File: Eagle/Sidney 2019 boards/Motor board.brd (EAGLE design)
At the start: 110 x 122 mm, 40 parts, among them IC2 LM2940CS-5.0_NOPB

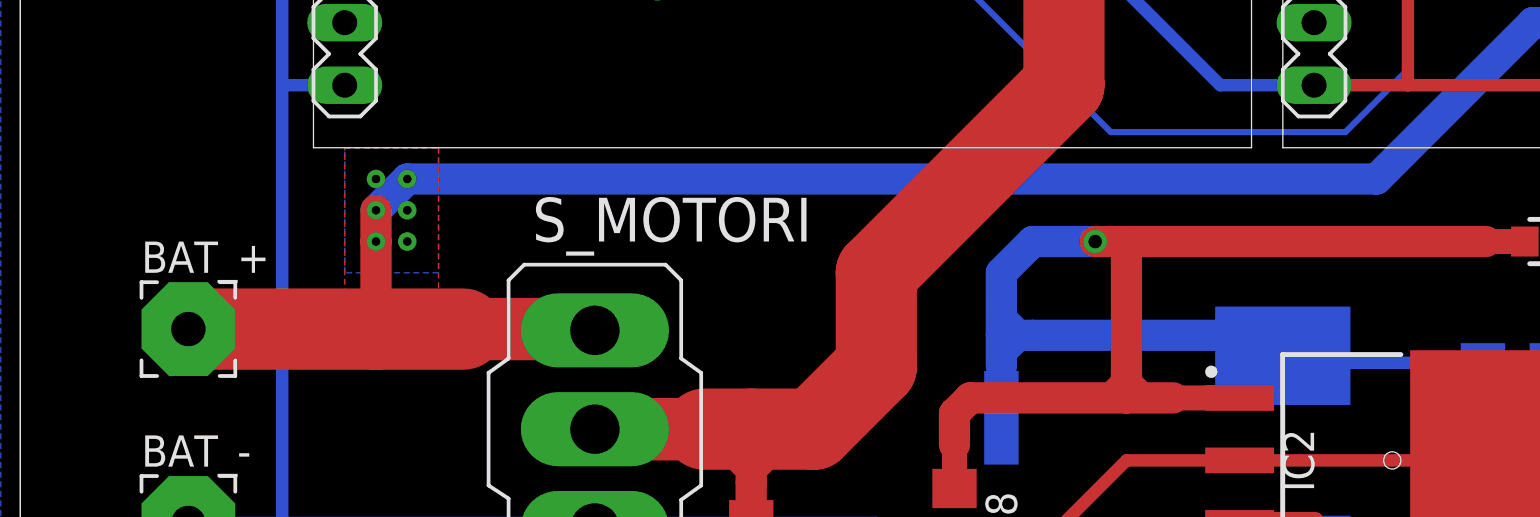
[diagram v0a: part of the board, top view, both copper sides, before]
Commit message: Fixed polygon near battery causing a short circuit
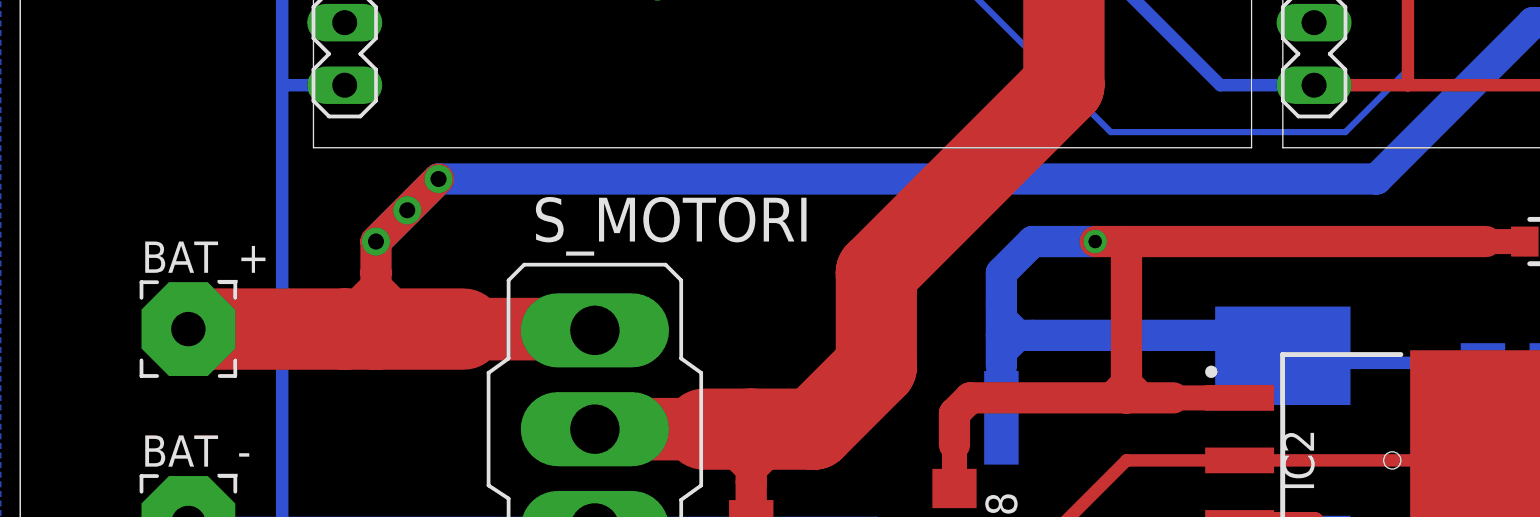
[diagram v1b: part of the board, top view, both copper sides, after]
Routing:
- net N$1: track 111.0 -> 117.8 mm
- removed copper zone on layer 1, net N$1
- removed copper zone on layer 16, net N$1
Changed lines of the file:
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@@
 <via x="55.88" y="80.01" extent="1-16" drill="0.35"/>
 <via x="114.3" y="73.66" extent="1-16" drill="0.35"/>
-<wire x1="116.84" y1="118.11" x2="105.41" y2="119.38" width="0" layer="19" extent="1-1"/>
-<wire x1="114.3" y1="73.66" x2="114.3" y2="72.39" width="0" layer="19" extent="16-16"/>
-<wire x1="90.17" y1="119.38" x2="85.09" y2="111.76" width="0" layer="19" extent="16-16"/>
-<wire x1="55.88" y1="80.01" x2="43.18" y2="81.28" width="0" layer="19" extent="1-1"/>
-<wire x1="52.07" y1="123.19" x2="58.42" y2="111.76" width="0" layer="19" extent="1-1"/>
 <via x="113.03" y="72.39" extent="1-16" drill="0.35"/>
 <via x="114.3" y="72.39" extent="1-16" drill="0.35"/>
@@
 <wire x1="116.84" y1="73.66" x2="116.84" y2="67.31" width="1.27" layer="16"/>
 <contactref element="BAT_+" pad="1"/>
-<wire x1="36.83" y1="66.294" x2="44.45" y2="66.294" width="3.302" layer="1"/>
+<wire x1="36.83" y1="66.294" x2="43.18" y2="66.294" width="3.302" layer="1"/>
+<wire x1="43.18" y1="66.294" x2="44.45" y2="66.294" width="3.302" layer="1"/>
 <wire x1="44.45" y1="66.294" x2="48.006" y2="66.294" width="3.302" layer="1"/>
 <wire x1="48.006" y1="66.294" x2="53.2892" y2="66.294" width="2.54" layer="1"/>
 <wire x1="53.2892" y1="66.294" x2="53.34" y2="66.2432" width="2.54" layer="1"/>
 <wire x1="91.44" y1="78.74" x2="85.09" y2="72.39" width="1.27" layer="16"/>
-<wire x1="44.45" y1="69.85" x2="44.45" y2="66.294" width="1.27" layer="1"/>
-<wire x1="85.09" y1="72.39" x2="45.72" y2="72.39" width="1.27" layer="16"/>
-<polygon width="0.1524" layer="1">
-<vertex x="43.18" y="73.66"/>
-<vertex x="46.99" y="73.66"/>
-<vertex x="46.99" y="67.31"/>
-<vertex x="43.18" y="67.31"/>
-</polygon>
-<polygon width="0.1524" layer="16">
-<vertex x="43.18" y="73.66"/>
-<vertex x="46.99" y="73.66"/>
-<vertex x="46.99" y="68.58"/>
-<vertex x="43.18" y="68.58"/>
-</polygon>
-<via x="45.72" y="72.39" extent="1-16" drill="0.35"/>
-<via x="44.45" y="69.85" extent="1-16" drill="0.35"/>
-<wire x1="45.72" y1="72.39" x2="44.45" y2="71.12" width="1.27" layer="16"/>
-<via x="44.45" y="71.12" extent="1-16" drill="0.35"/>
-<wire x1="44.45" y1="71.12" x2="44.45" y2="69.85" width="1.27" layer="1"/>
+<wire x1="85.09" y1="72.39" x2="46.99" y2="72.39" width="1.27" layer="16"/>
+<wire x1="46.99" y1="72.39" x2="45.72" y2="71.12" width="1.27" layer="16"/>
+<via x="44.45" y="69.85" extent="1-16" drill="0.65" diameter="1.15"/>
+<wire x1="45.72" y1="71.12" x2="44.45" y2="69.85" width="1.27" layer="16"/>
+<wire x1="44.45" y1="66.294" x2="44.45" y2="68.58" width="1.27" layer="1"/>
+<wire x1="44.45" y1="69.85" x2="44.45" y2="68.58" width="1.27" layer="1"/>
+<wire x1="44.45" y1="69.85" x2="45.72" y2="71.12" width="1.27" layer="1"/>
+<via x="46.99" y="72.39" extent="1-16" drill="0.65" diameter="1.15"/>
+<wire x1="45.72" y1="71.12" x2="46.99" y2="72.39" width="1.27" layer="1"/>
+<via x="45.72" y="71.12" extent="1-16" drill="0.65" diameter="1.15"/>
+<wire x1="43.18" y1="66.294" x2="43.18" y2="67.31" width="0.508" layer="1"/>
+<wire x1="43.18" y1="67.31" x2="44.45" y2="68.58" width="0.508" layer="1"/>
+<wire x1="44.45" y1="68.58" x2="45.212" y2="67.818" width="0.508" layer="1"/>
 </signal>
 <signal name="VCC">
@@
 <wire x1="128.27" y1="125.73" x2="100.33" y2="153.67" width="0.254" layer="16"/>
 </signal>
-<signal name="N$4">
-<via x="45.72" y="69.85" extent="1-16" drill="0.35"/>
-</signal>
-<signal name="N$5">
-<via x="45.72" y="71.12" extent="1-16" drill="0.35"/>
-</signal>
-<signal name="N$8">
-<via x="44.45" y="72.39" extent="1-16" drill="0.35"/>
-</signal>
 </signals>

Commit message: Started working on line sensors's 3.3V supply
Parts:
- added IC3: LM3940IS-3.3, LM3940IS-3.3:TO254P1435X457-4N
- moved SUPPLY2_CON 2.84 mm to (133.3, 90.2)
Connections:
- new net 3,3V/LS: IC3.3, S1.1, S2.1, S3.1, S4.1
- net +5V/S: now also IC3.1; no longer S1.1, S2.1, S3.1, S4.1
- net GND: now also IC3.2, IC3.4
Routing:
- net 3,3V/LS: track 0.00 -> 103.9 mm
- net +5V/S: track 440.5 -> 354.2 mm
- net GND: track 646.6 -> 667.6 mm
- net +5V: track 86.6 -> 85.8 mm

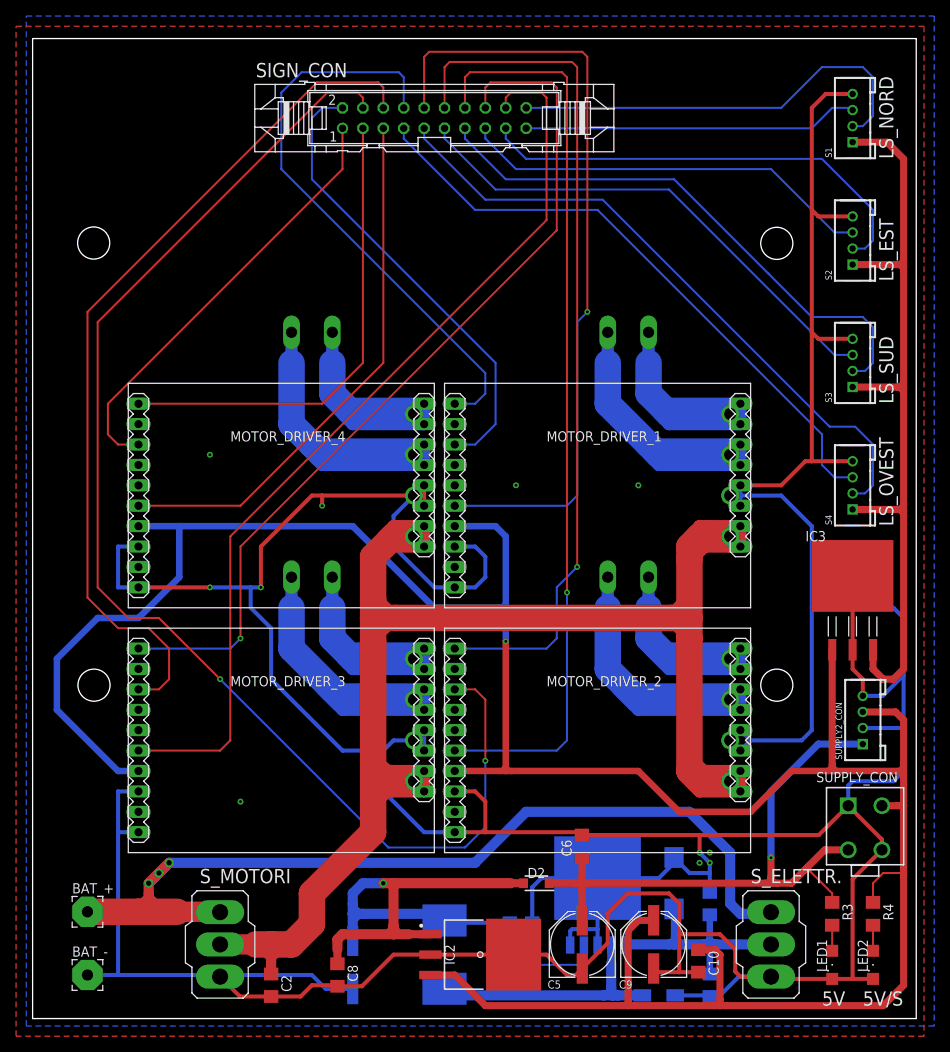
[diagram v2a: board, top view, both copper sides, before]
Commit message: Working on vias, removed empty portions of the motor board, added 3,3V LDO regulator for line sensors
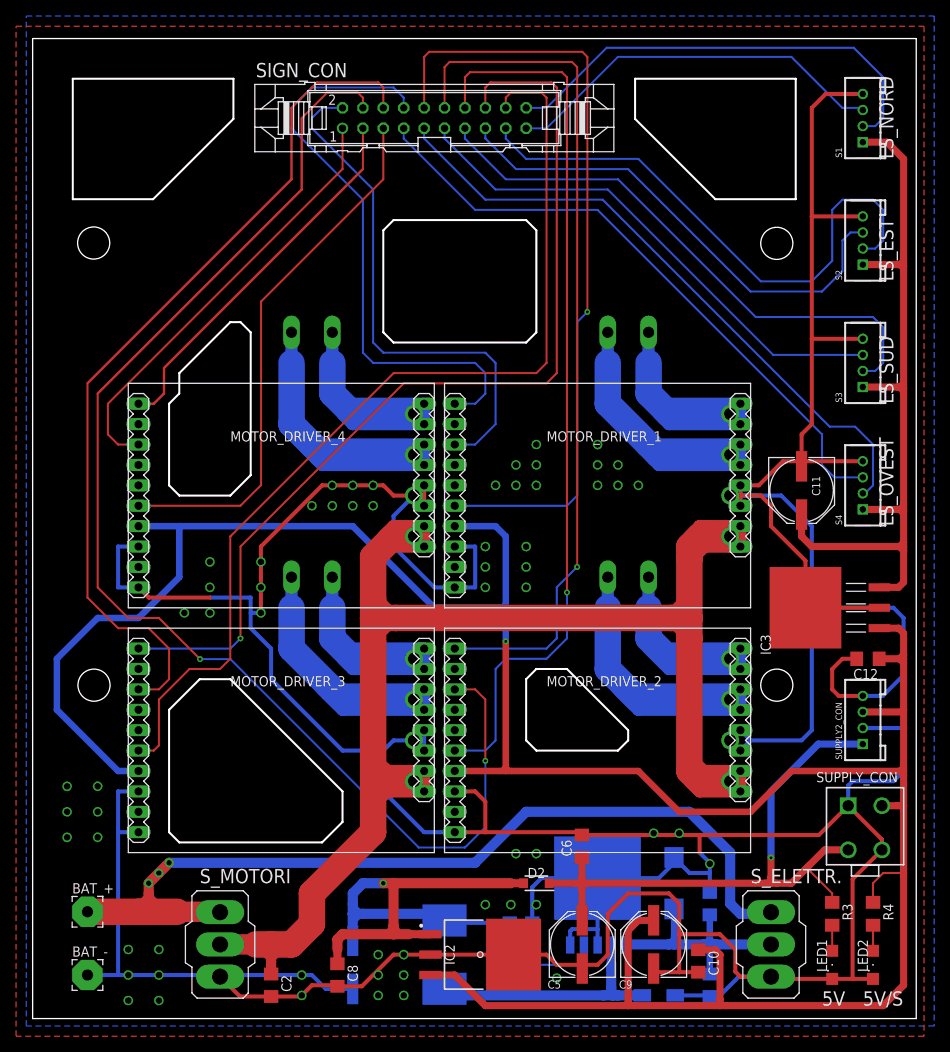
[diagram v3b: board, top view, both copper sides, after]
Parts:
- added C11: (no value), rcl:PANASONIC_E
- added C12: 100nF, rcl:C1206
- moved IC3 6.87 mm to (126.4, 104.1), turned to 90 degrees
- moved S1 1.27 mm to (133.3, 165.1)
- moved S2 1.27 mm to (133.3, 149.9)
- moved S3 1.27 mm to (133.3, 134.6)
- moved S4 1.27 mm to (133.3, 119.4)
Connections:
- net +5V/S: now also C12.1
- net 3,3V/LS: now also C11.+
- net GND: now also C11.-, C12.2
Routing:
- net GND: track 667.6 -> 700.2 mm, vias 11 -> 61
- net S2_IN: track 57.4 -> 70.8 mm
- net M4_INA: track 59.3 -> 47.0 mm
- net M3_INA: track 110.1 -> 120.5 mm
- net S2_OUT: track 51.8 -> 61.4 mm
- net M3_INB: track 115.1 -> 123.0 mm
- net M1_PWM: track 58.0 -> 65.5 mm
- net S1_OUT: track 41.8 -> 48.3 mm
- net S1_IN: track 53.7 -> 57.1 mm
- net 3,3V/LS: track 103.9 -> 101.4 mm
- net M2_INB: track 114.1 -> 111.9 mm
- net M1_INA: track 72.7 -> 74.1 mm
- net S3_IN: track 69.2 -> 70.5 mm
- net S4_OUT: track 76.9 -> 78.1 mm
- net S4_IN: track 81.0 -> 79.7 mm
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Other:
- outline, holes or cut-outs redrawn
